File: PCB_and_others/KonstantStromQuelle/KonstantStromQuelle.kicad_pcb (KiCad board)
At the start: 2 copper layers, 12 parts, among them J1 Konstantstromquelle, J2 +5V, J3 Halte-Pin, Q1 BSS138, U1 LM4041DIM3-1.2, U2 SGM8521

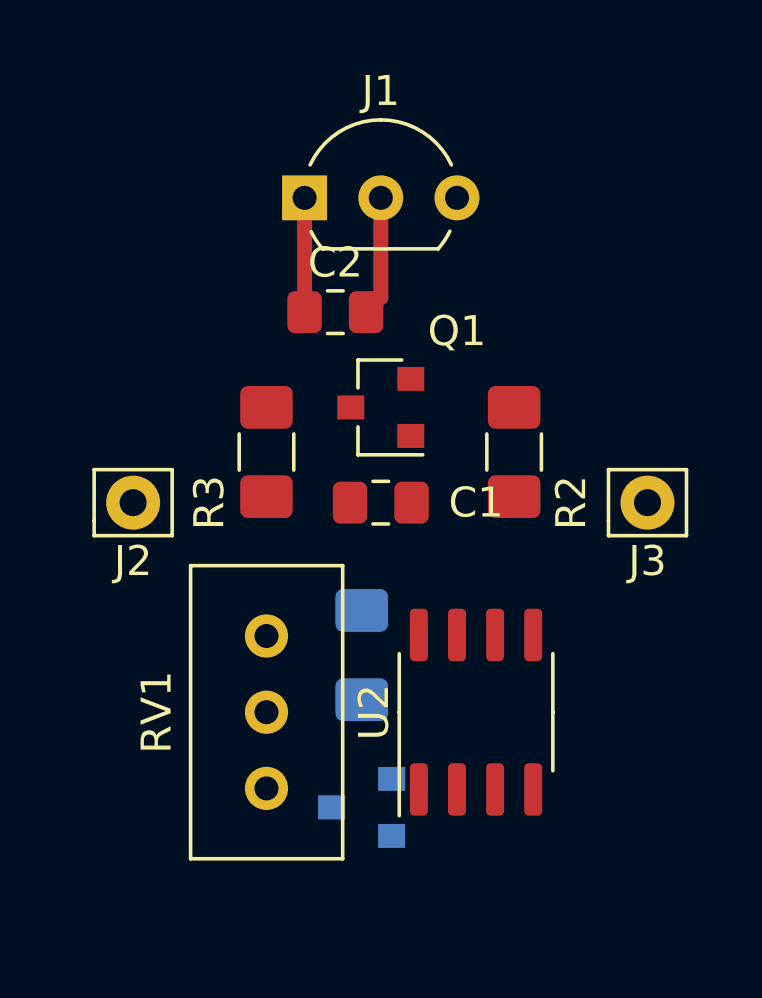
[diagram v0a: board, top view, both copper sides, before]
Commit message: Strart FlashWrite and PCB Ver.1.1 is ready
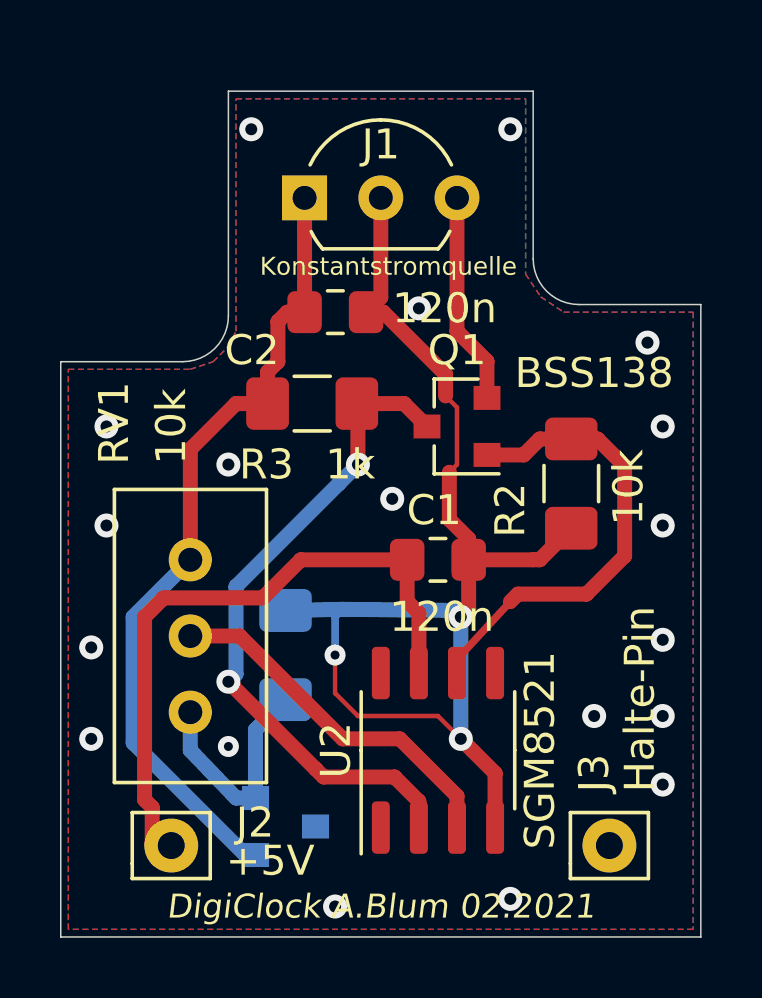
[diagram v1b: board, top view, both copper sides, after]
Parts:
- moved J3 11.5 mm to (135.9, 81.3)
- moved J2 11.5 mm to (121.3, 81.3)
- moved RV1 3.59 mm to (121.9, 71.8)
- moved C1 2.69 mm to (130.2, 71.8)
- moved U1 2.62 mm to (125.1, 80.6), turned to 0 degrees
- moved Q1 2.62 mm to (130.8, 67.3)
- moved R1 2.54 mm to (125.1, 74.9)
- moved R3 2.22 mm to (126.0, 66.5), turned to 0 degrees
- moved R2 2.18 mm to (134.6, 69.2)
- moved U2 1.80 mm to (130.2, 78.1)
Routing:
- net GNDA: track 4.01 -> 41.2 mm, vias 0 -> 22
- net +5V: track 0.00 -> 23.6 mm
- net +3V3: track 3.81 -> 27.1 mm
- net Net-(Q1-Pad3): track 0.00 -> 22.6 mm, vias 0 -> 2
- net Net-(Q1-Pad1): track 0.00 -> 15.7 mm
- net Net-(RV1-Pad2): track 0.00 -> 12.2 mm
- net Net-(R1-Pad1): track 0.00 -> 7.82 mm
- net Net-(J1-Pad3): track 0.00 -> 7.08 mm
- added copper zone on B.Cu, net GNDA
- added copper zone on F.Cu, net GNDA
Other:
- board outline added: 21.3 x 28.2 mm
- rule trace_min: 0.2 -> 0.127
- board text added: "DigiClock A.Blum 02.2021"
